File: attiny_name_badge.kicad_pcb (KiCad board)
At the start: 2 copper layers, 100.1 x 75.2 mm, 1 part, among them U1 ATtiny841-SSU

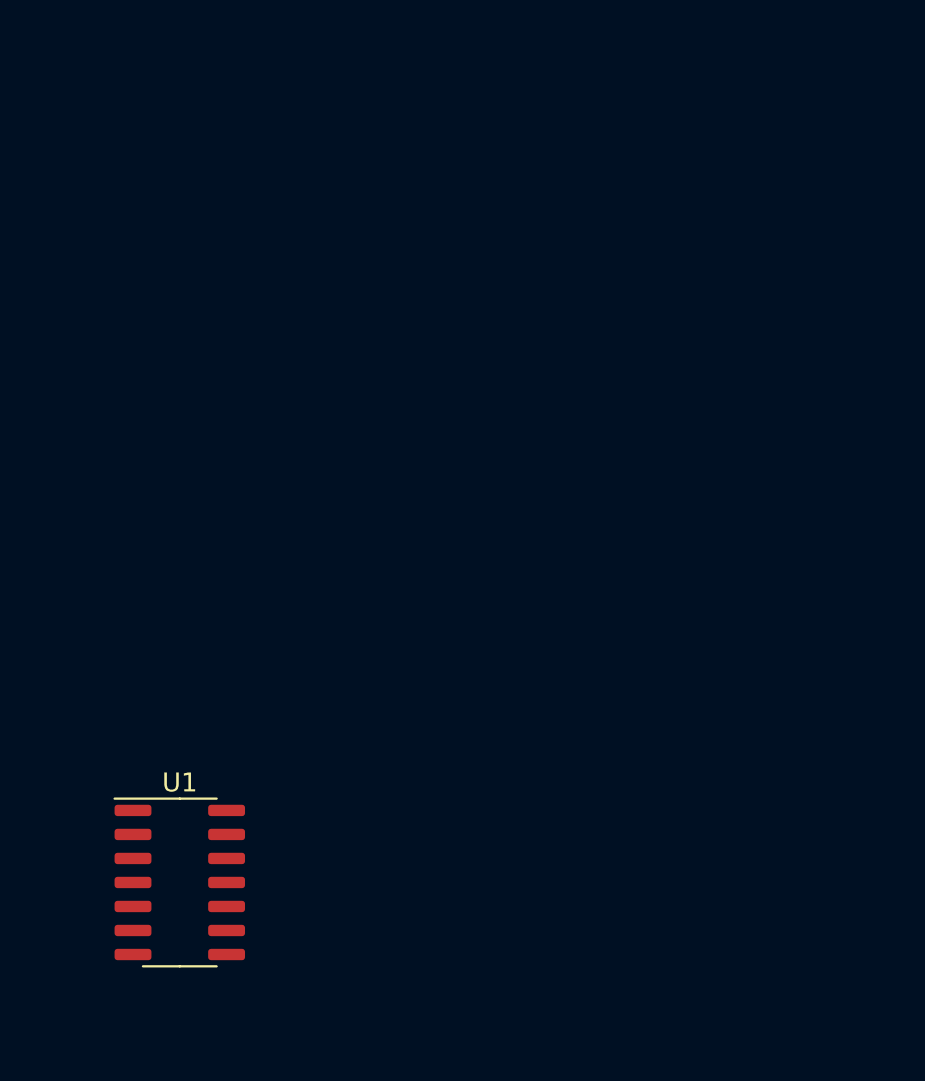
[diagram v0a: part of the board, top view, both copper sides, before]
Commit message: initial layout
custom 2032 cell holder
misc initial placements
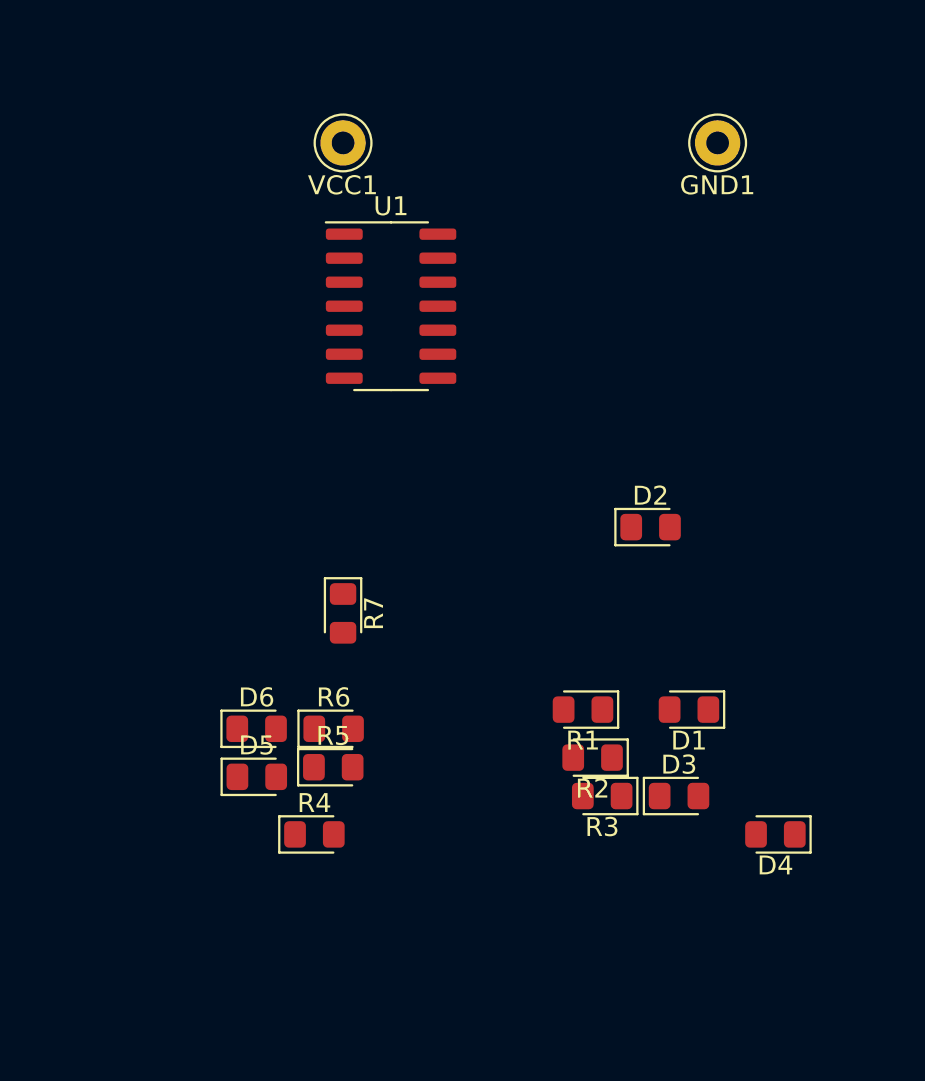
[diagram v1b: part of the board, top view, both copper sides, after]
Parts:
- added D1: LED, LED_SMD:LED_0805_2012Metric_Pad1.15x1.40mm_HandSolder, F.Cu at (90.9, 104.6)
- added D2: LED, LED_SMD:LED_0805_2012Metric_Pad1.15x1.40mm_HandSolder, F.Cu at (88.9, 95.0)
- added D3: LED, LED_SMD:LED_0805_2012Metric_Pad1.15x1.40mm_HandSolder, F.Cu at (90.4, 109.2)
- added D4: LED, LED_SMD:LED_0805_2012Metric_Pad1.15x1.40mm_HandSolder, F.Cu at (95.5, 111.3)
- added D5: LED, LED_SMD:LED_0805_2012Metric_Pad1.15x1.40mm_HandSolder, F.Cu at (68.1, 108.2)
- added D6: LED, LED_SMD:LED_0805_2012Metric_Pad1.15x1.40mm_HandSolder, F.Cu at (68.1, 105.7)
- added GND1: Conn_01x01_Female, Connector_Pin:Pin_D1.0mm_L10.0mm_LooseFit, F.Cu at (92.5, 74.7)
- added R1: R_Small_US, LED_SMD:LED_0805_2012Metric_Pad1.15x1.40mm_HandSolder, F.Cu at (85.3, 104.6)
- added R2: R_Small_US, LED_SMD:LED_0805_2012Metric_Pad1.15x1.40mm_HandSolder, F.Cu at (85.8, 107.2)
- added R3: R_Small_US, LED_SMD:LED_0805_2012Metric_Pad1.15x1.40mm_HandSolder, F.Cu at (86.4, 109.2)
- added R4: R_Small_US, LED_SMD:LED_0805_2012Metric_Pad1.15x1.40mm_HandSolder, F.Cu at (71.1, 111.3)
- added R5: R_Small_US, LED_SMD:LED_0805_2012Metric_Pad1.15x1.40mm_HandSolder, F.Cu at (72.1, 107.7)
- added R6: R_Small_US, LED_SMD:LED_0805_2012Metric_Pad1.15x1.40mm_HandSolder, F.Cu at (72.1, 105.7)
- added R7: 10k, LED_SMD:LED_0805_2012Metric_Pad1.15x1.40mm_HandSolder, F.Cu at (72.6, 99.6)
- added VCC1: Conn_01x01_Female, Connector_Pin:Pin_D1.0mm_L10.0mm_LooseFit, F.Cu at (72.6, 74.7)
- moved U1 32.5 mm to (75.2, 83.3)
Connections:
- U1 pad 1: Net-(U1-Pad1) -> VCC
- U1 pad 14: Net-(U1-Pad14) -> GND

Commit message: working circuit
need name/finishing touches
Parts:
- added C1: CAP0805, Capacitor_SMD:C_0805_2012Metric_Pad1.15x1.40mm_HandSolder, F.Cu at (187.3, 104.8)
- added D10: LED, LED_SMD:LED_0805_2012Metric_Pad1.15x1.40mm_HandSolder, F.Cu at (162.6, 90.2)
- added D11: LED, LED_SMD:LED_0805_2012Metric_Pad1.15x1.40mm_HandSolder, F.Cu at (172.7, 90.2)
- added D12: LED, LED_SMD:LED_0805_2012Metric_Pad1.15x1.40mm_HandSolder, F.Cu at (182.9, 90.2)
- added D7: LED, LED_SMD:LED_0805_2012Metric_Pad1.15x1.40mm_HandSolder, F.Cu at (201.9, 90.2)
- added D8: LED, LED_SMD:LED_0805_2012Metric_Pad1.15x1.40mm_HandSolder, F.Cu at (212.1, 90.2)
- added D9: LED, LED_SMD:LED_0805_2012Metric_Pad1.15x1.40mm_HandSolder, F.Cu at (222.2, 90.2)
- moved R3 134.1 mm to (219.7, 95.2)
- moved D3 128.2 mm to (217.2, 90.2), turned to 270 degrees
- moved R2 124.3 mm to (209.6, 95.2)
- moved D6 120.9 mm to (188.0, 90.2), turned to 270 degrees
- moved U1 120.6 mm to (192.4, 111.8)
- moved D2 118.2 mm to (207.0, 90.2), turned to 270 degrees
- moved R7 115.1 mm to (187.3, 109.5)
- moved VCC1 114.4 mm to (182.4, 107.2)
- moved GND1 114.4 mm to (202.2, 107.2)
- moved R1 114.4 mm to (199.4, 95.2)
- moved R6 113.8 mm to (185.4, 95.2)
- moved D5 111.2 mm to (177.8, 90.2), turned to 270 degrees
- moved D1 106.9 mm to (196.8, 90.2), turned to 270 degrees
- moved R5 103.9 mm to (175.3, 95.2)
- moved R4 95.3 mm to (165.1, 95.2)
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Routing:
- net GND: track 0.00 -> 96.6 mm
- net Net-(R3-Pad2): track 0.00 -> 39.5 mm
- net Net-(R4-Pad2): track 0.00 -> 39.5 mm
- net Net-(R5-Pad2): track 0.00 -> 28.8 mm
- net Net-(R2-Pad2): track 0.00 -> 28.8 mm
- net Net-(R6-Pad2): track 0.00 -> 28.7 mm
- net Net-(R1-Pad2): track 0.00 -> 28.7 mm
- net VCC: track 0.00 -> 10.9 mm
- net Net-(D2-Pad2): track 0.00 -> 9.76 mm
- net Net-(D12-Pad2): track 0.00 -> 9.76 mm
- net Net-(D11-Pad2): track 0.00 -> 9.76 mm
- net Net-(D1-Pad2): track 0.00 -> 9.76 mm
- net Net-(D3-Pad2): track 0.00 -> 9.76 mm
- net Net-(D10-Pad2): track 0.00 -> 9.76 mm
- net Net-(R7-Pad2): track 0.00 -> 3.13 mm
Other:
- board outline removed

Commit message: working board
cut 'er out!
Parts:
- added G***: LOGO, LOGO, F.Cu at (193.0, 84.5)
- added G***: LOGO, LOGO, F.Cu at (186.7, 66.0)
- added G***: LOGO, LOGO, F.Cu at (205.7, 69.8)
- added SW1: SW_DPST_x2, Button_Switch_THT:SW_PUSH_6mm_H5mm, F.Cu at (197.5, 104.1)
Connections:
- U1 pad 1: VCC -> Net-(SW1-Pad1)
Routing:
- net VCC: track 10.9 -> 22.5 mm
- net Net-(SW1-Pad1): track 0.00 -> 10.7 mm
- net GND: track 96.6 -> 101.4 mm
- net (no net): vias 0 -> 1
- added copper zone on B.Cu, net (none)
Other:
- board outline added: 72.4 x 72.4 mm
